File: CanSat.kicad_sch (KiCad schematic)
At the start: 44 parts, among them IC1 W25Q128JVPIQ, J1 USB_C_Receptacle, J10 Conn_01x04_Pin, J2 Conn_Coaxial, J3 Conn_01x06_Socket, J4 Conn_01x02_Pin, J5 Screw_Terminal_01x02, J6 Conn_01x06_Pin, J7 Conn_01x03_Pin, J8 Conn_01x02_Pin, J9 Conn_01x02_Pin, SW1 SW_Push, SW2 SW_Push, U1 MPU-6050, U3 Waveshare23721, U4 RFM98W-433S2, U8 BMP280, U9 APS6404L-3SQR-ZR

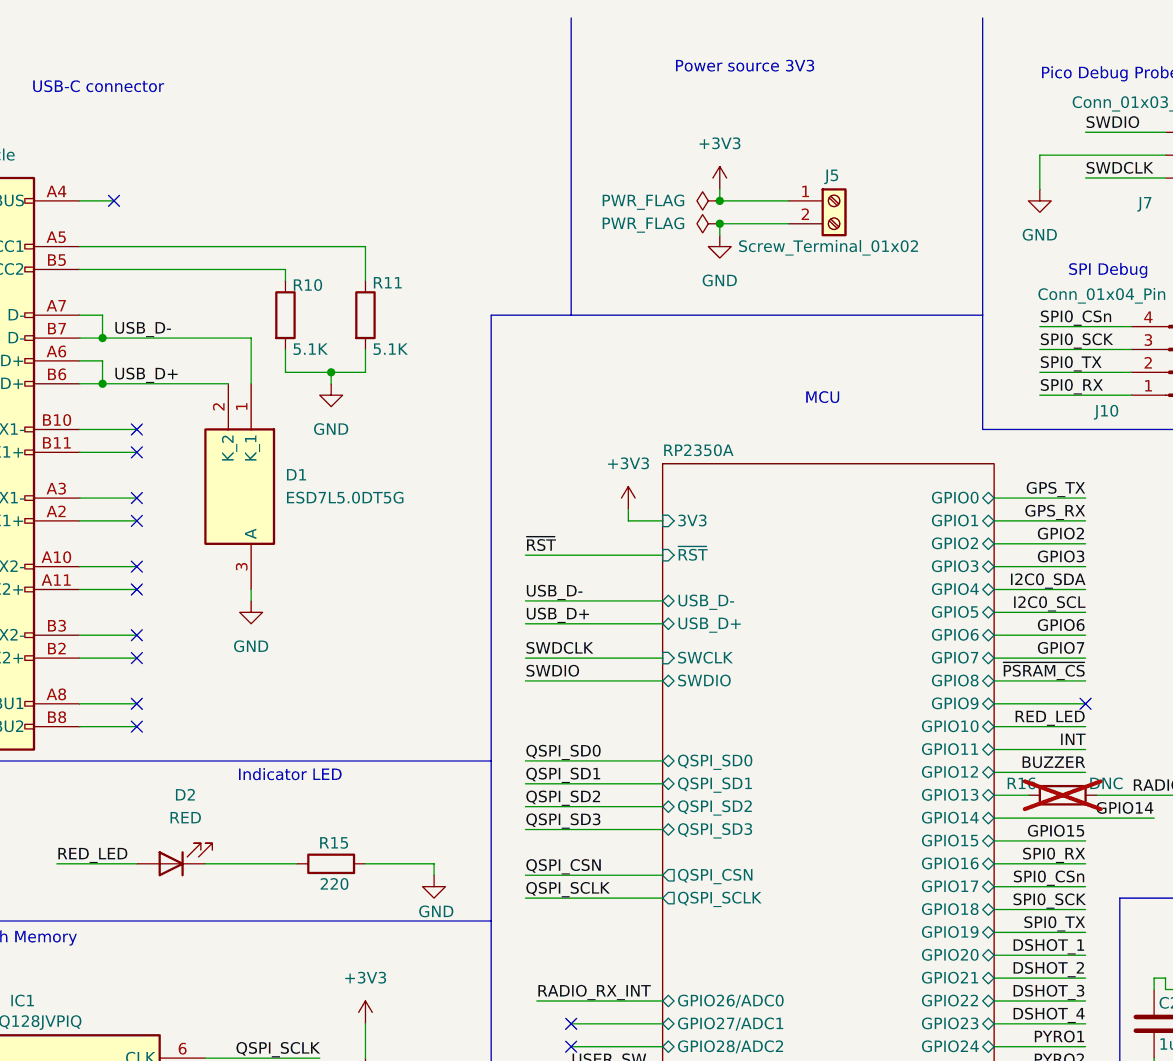
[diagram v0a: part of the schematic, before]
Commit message: Changed LoRa footprint + signed the PCB + added a on/off button
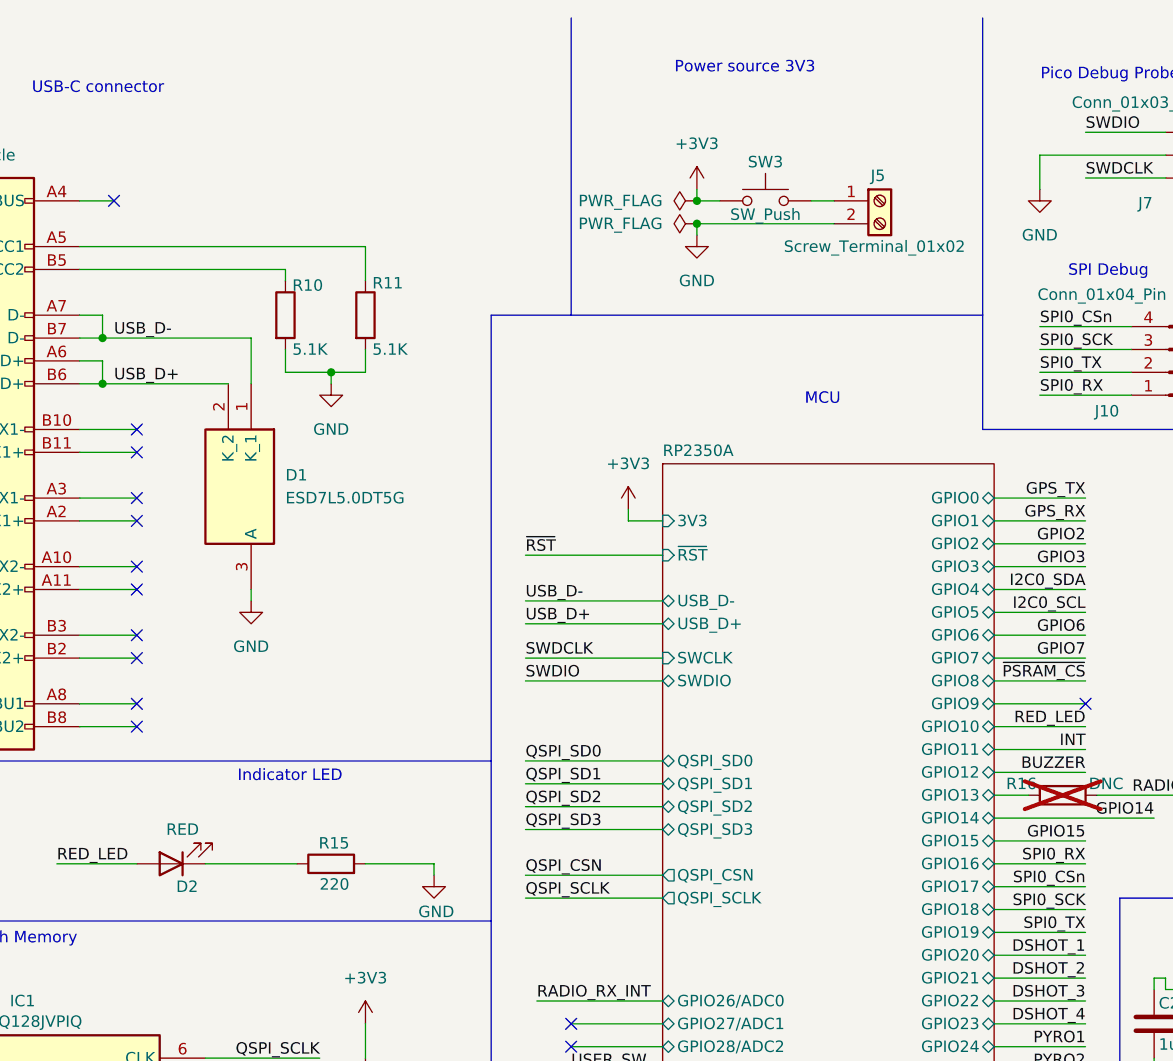
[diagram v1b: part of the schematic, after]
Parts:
- added SW3: SW_Push, Button_Switch_SMD:SW_Push_1P1T_NO_Vertical_Wuerth_434133025816, symbol Switch:SW_Push
- U4: footprint RF_Module:HOPERF_RFM9XW_THT -> RF_Module:HOPERF_RFM9XW_SMD
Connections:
- net +3V3: now also SW3.1; no longer J5.1 (Pin_1)
- new net: J5.1 (Pin_1), SW3.2
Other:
- moved on the sheet: J5
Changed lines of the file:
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@@
 	(title_block
 		(title "Main Board")
-		(date "2026-01-26")
-		(rev "v2.0.0")
+		(date "2026-03-07")
+		(rev "v2.1.0")
 		(company "Team ApolLO")
 		(comment 1 "Author: Wiktor Kociuba")
@@
 	)
 	(junction
-		(at 123.19 35.56)
+		(at 120.65 35.56)
 		(diameter 0)
 		(color 0 0 0 0)
@@
 	)
 	(junction
-		(at 123.19 33.02)
-		(diameter 0)
-		(color 0 0 0 0)
-	)
-	(junction
 		(at 179.07 120.65)
 		(diameter 0)
@@
 	)
 	(junction
+		(at 120.65 33.02)
+		(diameter 0)
+		(color 0 0 0 0)
+	)
+	(junction
 		(at 233.68 120.65)
 		(diameter 0)
@@
 	(wire
 		(pts
-			(xy 123.19 31.75) (xy 123.19 33.02)
+			(xy 120.65 31.75) (xy 120.65 33.02)
 		)
 		(stroke
@@
 	(wire
 		(pts
-			(xy 123.19 35.56) (xy 123.19 36.83)
+			(xy 120.65 35.56) (xy 120.65 36.83)
 		)
 		(stroke
@@
 	(wire
 		(pts
+			(xy 133.35 33.02) (xy 135.89 33.02)
+		)
+		(stroke
+			(width 0)
+			(type default)
+		)
+	)
+	(wire
+		(pts
 			(xy 247.65 158.75) (xy 245.11 158.75)
 		)
@@
 	(wire
 		(pts
-			(xy 123.19 33.02) (xy 130.81 33.02)
-		)
-		(stroke
-			(width 0)
-			(type default)
-		)
-	)
-	(wire
-		(pts
 			(xy 185.42 30.48) (xy 193.04 30.48)
 		)
@@
 	(wire
 		(pts
+			(xy 120.65 33.02) (xy 123.19 33.02)
+		)
+		(stroke
+			(width 0)
+			(type default)
+		)
+	)
+	(wire
+		(pts
 			(xy 213.36 86.36) (xy 213.36 93.98)
 		)
@@
 	(wire
 		(pts
-			(xy 123.19 35.56) (xy 130.81 35.56)
+			(xy 120.65 35.56) (xy 135.89 35.56)
 		)
 		(stroke
@@
 	(symbol
 		(lib_id "power:GND")
-		(at 123.19 36.83 0)
+		(at 120.65 36.83 0)
 		(unit 1)
 		(exclude_from_sim no)
@@
 		(fields_autoplaced yes)
 		(property "Reference" "#PWR07"
-			(at 123.19 43.18 0)
+			(at 120.65 43.18 0)
 			(effects
 				(font
@@
 		)
 		(property "Value" "GND"
-			(at 123.19 41.91 0)
+			(at 120.65 41.91 0)
 			(effects
 				(font
@@
 		)
 		(property "Footprint" ""
-			(at 123.19 36.83 0)
+			(at 120.65 36.83 0)
 			(effects
 				(font
@@
 		)
 		(property "Datasheet" ""
-			(at 123.19 36.83 0)
+			(at 120.65 36.83 0)
 			(effects
 				(font
@@
 		)
 		(property "Description" "Power symbol creates a global label with name \"GND\" , ground"
-			(at 123.19 36.83 0)
+			(at 120.65 36.83 0)
 			(effects
 				(font
@@
 	(symbol
 		(lib_id "Connector:Screw_Terminal_01x02")
-		(at 135.89 33.02 0)
+		(at 140.97 33.02 0)
 		(unit 1)
 		(exclude_from_sim no)
@@
 		(dnp no)
 		(property "Reference" "J5"
-			(at 134.874 30.226 0)
+			(at 139.954 30.226 0)
 			(effects
 				(font
@@
 		)
 		(property "Value" "Screw_Terminal_01x02"
-			(at 125.222 38.1 0)
+			(at 130.302 38.1 0)
 			(effects
 				(font
@@
 		)
 		(property "Footprint" "TerminalBlock:TerminalBlock_bornier-2_P5.08mm"
-			(at 135.89 33.02 0)
+			(at 140.97 33.02 0)
 			(effects
 				(font
@@
 		)
 		(property "Datasheet" "~"
-			(at 135.89 33.02 0)
+			(at 140.97 33.02 0)
 			(effects
 				(font
@@
 		)
 		(property "Description" "Generic screw terminal, single row, 01x02, script generated (kicad-library-utils/schlib/autogen/connector/)"
-			(at 135.89 33.02 0)
+			(at 140.97 33.02 0)
 			(effects
 				(font
@@
 		(on_board yes)
 		(dnp no)
-		(fields_autoplaced yes)
 		(property "Reference" "D2"
-			(at 63.8175 99.06 0)
+			(at 64.008 109.22 0)
 			(effects
 				(font
@@
 		)
 		(property "Value" "RED"
-			(at 63.8175 101.6 0)
+			(at 63.5 102.87 0)
 			(effects
 				(font
@@
 			)
 		)
-		(property "Footprint" "RF_Module:HOPERF_RFM9XW_THT"
+		(property "Footprint" "RF_Module:HOPERF_RFM9XW_SMD"
 			(at 161.29 100.33 0)
 			(effects
@@
 	(symbol
 		(lib_id "power:PWR_FLAG")
-		(at 123.19 35.56 90)
+		(at 120.65 35.56 90)
 		(unit 1)
 		(exclude_from_sim no)
@@
 		(fields_autoplaced yes)
 		(property "Reference" "#FLG02"
-			(at 121.285 35.56 0)
+			(at 118.745 35.56 0)
 			(effects
 				(font
@@
 		)
 		(property "Value" "PWR_FLAG"
-			(at 119.38 35.5599 90)
+			(at 116.84 35.5599 90)
 			(effects
 				(font
@@
 		)
 		(property "Footprint" ""
-			(at 123.19 35.56 0)
+			(at 120.65 35.56 0)
 			(effects
 				(font
@@
 		)
 		(property "Datasheet" "~"
-			(at 123.19 35.56 0)
+			(at 120.65 35.56 0)
 			(effects
 				(font
@@
 		)
 		(property "Description" "Special symbol for telling ERC where power comes from"
-			(at 123.19 35.56 0)
+			(at 120.65 35.56 0)
 			(effects
 				(font
@@
 	)
 	(symbol
+		(lib_id "Switch:SW_Push")
+		(at 128.27 33.02 0)
+		(unit 1)
+		(exclude_from_sim no)
+		(in_bom yes)
+		(on_board yes)
+		(dnp no)
+		(property "Reference" "SW3"
+			(at 128.27 28.702 0)
+			(effects
+				(font
+					(size 1.27 1.27)
+				)
+			)
+		)
+		(property "Value" "SW_Push"
+			(at 128.27 34.544 0)
+			(effects
+				(font
+					(size 1.27 1.27)
+				)
+			)
+		)
+		(property "Footprint" "Button_Switch_SMD:SW_Push_1P1T_NO_Vertical_Wuerth_434133025816"
+			(at 128.27 27.94 0)
+			(effects
+				(font
+					(size 1.27 1.27)
+				)
+				(hide yes)
+			)
+		)
+		(property "Datasheet" "~"
+			(at 128.27 27.94 0)
+			(effects
+				(font
+					(size 1.27 1.27)
+				)
+				(hide yes)
+			)
+		)
+		(property "Description" "Push button switch, generic, two pins"
+			(at 128.27 33.02 0)
+			(effects
+				(font
+					(size 1.27 1.27)
+				)
+				(hide yes)
+			)
+		)
+		(pin "2"
+		)
+		(pin "1"
+		)
+		(instances
+			(project ""
+				(path "/c5feb985-eaed-4048-a722-7becddf33f05"
+					(reference "SW3")
+					(unit 1)
+				)
+			)
+		)
+	)
+	(symbol
 		(lib_id "power:+3V3")
 		(at 113.03 67.31 0)
@@
 	(symbol
 		(lib_id "power:+3V3")
-		(at 123.19 31.75 0)
+		(at 120.65 31.75 0)
 		(unit 1)
 		(exclude_from_sim no)
@@
 		(fields_autoplaced yes)
 		(property "Reference" "#PWR08"
-			(at 123.19 35.56 0)
+			(at 120.65 35.56 0)
 			(effects
 				(font
@@
 		)
 		(property "Value" "+3V3"
-			(at 123.19 26.67 0)
+			(at 120.65 26.67 0)
 			(effects
 				(font
@@
 		)
 		(property "Footprint" ""
-			(at 123.19 31.75 0)
+			(at 120.65 31.75 0)
 			(effects
 				(font
@@
 		)
 		(property "Datasheet" ""
-			(at 123.19 31.75 0)
+			(at 120.65 31.75 0)
 			(effects
 				(font
@@
 		)
 		(property "Description" "Power symbol creates a global label with name \"+3V3\""
-			(at 123.19 31.75 0)
+			(at 120.65 31.75 0)
 			(effects
 				(font
@@
 	(symbol
 		(lib_id "power:PWR_FLAG")
-		(at 123.19 33.02 90)
+		(at 120.65 33.02 90)
 		(unit 1)
 		(exclude_from_sim no)
@@
 		(fields_autoplaced yes)
 		(property "Reference" "#FLG01"
-			(at 121.285 33.02 0)
+			(at 118.745 33.02 0)
 			(effects
 				(font
@@
 		)
 		(property "Value" "PWR_FLAG"
-			(at 119.38 33.0199 90)
+			(at 116.84 33.0199 90)
 			(effects
 				(font
@@
 		)
 		(property "Footprint" ""
-			(at 123.19 33.02 0)
+			(at 120.65 33.02 0)
 			(effects
 				(font
@@
 		)
 		(property "Datasheet" "~"
-			(at 123.19 33.02 0)
+			(at 120.65 33.02 0)
 			(effects
 				(font
@@
 		)
 		(property "Description" "Special symbol for telling ERC where power comes from"
-			(at 123.19 33.02 0)
+			(at 120.65 33.02 0)
 			(effects
 				(font

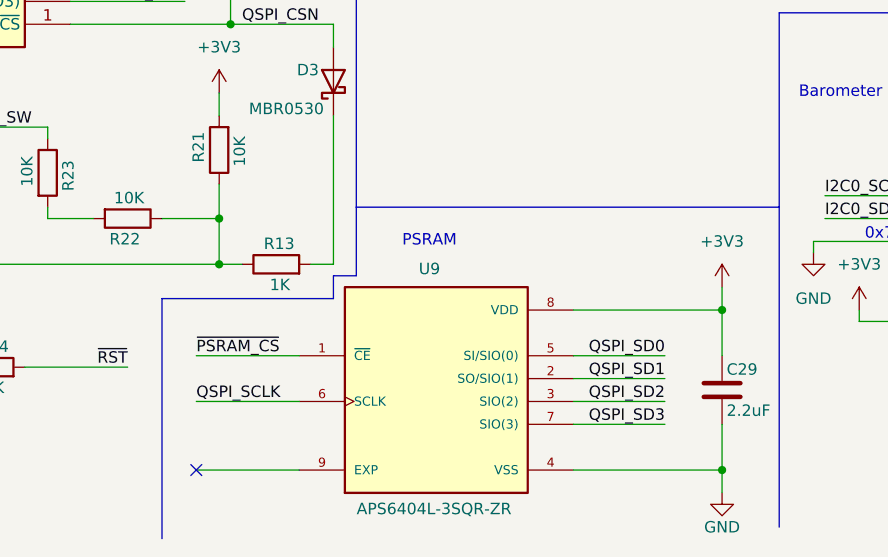
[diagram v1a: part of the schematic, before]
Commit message: Fixed design flaw with with components that MCU depends on
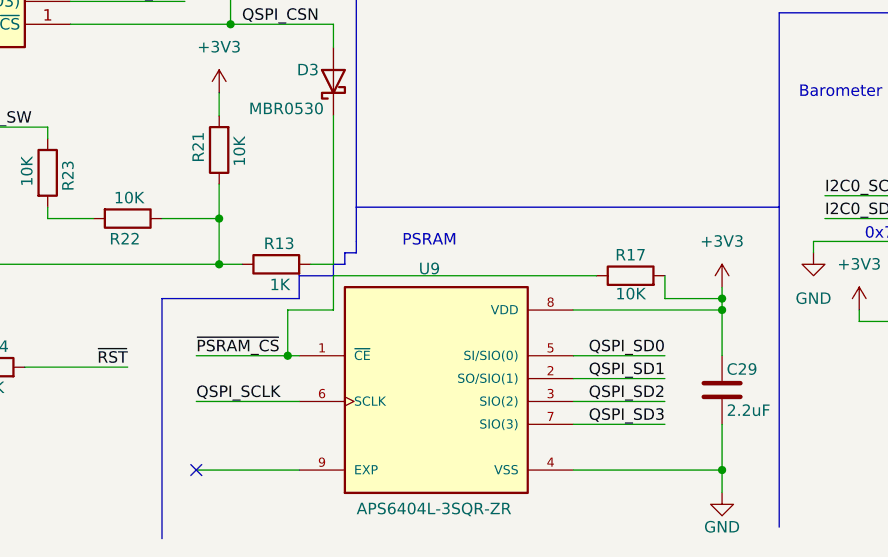
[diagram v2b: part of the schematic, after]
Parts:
- added R17: 10K, Resistor_SMD:R_0402_1005Metric, symbol Device:R
- BZ1: footprint Buzzer_Beeper:MagneticBuzzer_Kingstate_KCG0601 -> buzzer:CMT-4023S
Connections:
- net +3V3: now also R17.2
- net ~{PSRAM_CS}: now also R17.1
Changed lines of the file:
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@@
 	(title_block
 		(title "Main Board")
-		(date "2026-03-07")
-		(rev "v2.1.0")
+		(date "2026-03-11")
+		(rev "v2.1.1")
 		(company "Team ApolLO")
 		(comment 1 "Author: Wiktor Kociuba")
@@
 	)
 	(junction
+		(at 138.43 171.45)
+		(diameter 0)
+		(color 0 0 0 0)
+	)
+	(junction
 		(at 245.11 158.75)
 		(diameter 0)
@@
 	)
 	(junction
+		(at 90.17 177.8)
+		(diameter 0)
+		(color 0 0 0 0)
+	)
+	(junction
 		(at 82.55 167.64)
 		(diameter 0)
@@
 	(wire
 		(pts
+			(xy 132.08 168.91) (xy 132.08 171.45)
+		)
+		(stroke
+			(width 0)
+			(type default)
+		)
+	)
+	(wire
+		(pts
 			(xy 185.42 81.28) (xy 194.31 81.28)
 		)
@@
 	(wire
 		(pts
+			(xy 90.17 172.72) (xy 95.25 172.72)
+		)
+		(stroke
+			(width 0)
+			(type default)
+		)
+	)
+	(wire
+		(pts
 			(xy 66.04 138.43) (xy 78.74 138.43)
 		)
@@
 	(wire
 		(pts
+			(xy 95.25 168.91) (xy 124.46 168.91)
+		)
+		(stroke
+			(width 0)
+			(type default)
+		)
+	)
+	(wire
+		(pts
 			(xy 245.11 158.75) (xy 245.11 160.02)
 		)
@@
 	(polyline
 		(pts
-			(xy 76.2 171.45) (xy 95.25 171.45)
+			(xy 76.2 171.45) (xy 91.44 171.45)
 		)
 		(stroke
@@
 	(polyline
 		(pts
-			(xy 97.79 168.91) (xy 97.79 161.29)
+			(xy 97.79 165.1) (xy 97.79 161.29)
+		)
+		(stroke
+			(width 0)
+			(type default)
+		)
+	)
+	(polyline
+		(pts
+			(xy 96.52 166.37) (xy 97.79 166.37)
 		)
 		(stroke
@@
 	(polyline
 		(pts
-			(xy 95.25 171.45) (xy 95.25 168.91)
+			(xy 91.44 171.45) (xy 91.44 168.91)
 		)
 		(stroke
@@
 	(wire
 		(pts
+			(xy 138.43 171.45) (xy 138.43 172.72)
+		)
+		(stroke
+			(width 0)
+			(type default)
+		)
+	)
+	(wire
+		(pts
 			(xy 36.83 167.64) (xy 36.83 179.07)
 		)
@@
 	(wire
 		(pts
+			(xy 90.17 177.8) (xy 90.17 172.72)
+		)
+		(stroke
+			(width 0)
+			(type default)
+		)
+	)
+	(wire
+		(pts
 			(xy 170.18 175.26) (xy 170.18 176.53)
 		)
@@
 	(wire
 		(pts
-			(xy 80.01 177.8) (xy 91.44 177.8)
+			(xy 80.01 177.8) (xy 90.17 177.8)
 		)
 		(stroke
@@
 	(wire
 		(pts
+			(xy 95.25 172.72) (xy 95.25 168.91)
+		)
+		(stroke
+			(width 0)
+			(type default)
+		)
+	)
+	(wire
+		(pts
 			(xy 153.67 71.12) (xy 163.83 71.12)
 		)
@@
 		)
 	)
+	(polyline
+		(pts
+			(xy 95.25 168.91) (xy 95.25 167.64)
+		)
+		(stroke
+			(width 0)
+			(type default)
+		)
+	)
 	(wire
 		(pts
@@
 	(wire
 		(pts
+			(xy 90.17 177.8) (xy 91.44 177.8)
+		)
+		(stroke
+			(width 0)
+			(type default)
+		)
+	)
+	(wire
+		(pts
 			(xy 200.66 152.4) (xy 208.28 152.4)
 		)
@@
 	(wire
 		(pts
+			(xy 132.08 171.45) (xy 138.43 171.45)
+		)
+		(stroke
+			(width 0)
+			(type default)
+		)
+	)
+	(wire
+		(pts
 			(xy 24.13 138.43) (xy 22.86 138.43)
 		)
@@
 		)
 	)
-	(polyline
+	(wire
 		(pts
-			(xy 95.25 168.91) (xy 97.79 168.91)
+			(xy 185.42 27.94) (xy 193.04 27.94)
 		)
 		(stroke
@@
 		)
 	)
-	(wire
+	(polyline
 		(pts
-			(xy 185.42 27.94) (xy 193.04 27.94)
+			(xy 96.52 167.64) (xy 96.52 166.37)
 		)
 		(stroke
@@
 		)
 	)
+	(polyline
+		(pts
+			(xy 91.44 168.91) (xy 95.25 168.91)
+		)
+		(stroke
+			(width 0)
+			(type default)
+		)
+	)
 	(wire
 		(pts
@@
 		)
 	)
+	(polyline
+		(pts
+			(xy 95.25 167.64) (xy 96.52 167.64)
+		)
+		(stroke
+			(width 0)
+			(type default)
+		)
+	)
 	(wire
 		(pts
@@
 		)
 	)
+	(polyline
+		(pts
+			(xy 97.79 166.37) (xy 97.79 165.1)
+		)
+		(stroke
+			(width 0)
+			(type default)
+		)
+	)
 	(wire
 		(pts
@@
 	(wire
 		(pts
-			(xy 138.43 170.18) (xy 138.43 172.72)
+			(xy 138.43 170.18) (xy 138.43 171.45)
 		)
 		(stroke
@@
 			)
 		)
-		(property "Footprint" "Buzzer_Beeper:MagneticBuzzer_Kingstate_KCG0601"
+		(property "Footprint" "buzzer:CMT-4023S"
 			(at 266.065 25.4 90)
 			(effects
@@
 					(unit 1)
 				)
+			)
+		)
+	)
+	(symbol
+		(lib_id "Device:R")
+		(at 128.27 168.91 90)
+		(unit 1)
+		(exclude_from_sim no)
+		(in_bom yes)
+		(on_board yes)
+		(dnp no)
+		(property "Reference" "R17"
+			(at 128.27 166.624 90)
+			(effects
+				(font
+					(size 1.27 1.27)
+				)
+			)
+		)
+		(property "Value" "10K"
+			(at 128.27 170.942 90)
+			(effects
+				(font
+					(size 1.27 1.27)
+				)
+			)
+		)
+		(property "Footprint" "Resistor_SMD:R_0402_1005Metric"
+			(at 128.27 170.688 90)
+			(effects
+				(font
+					(size 1.27 1.27)
+				)
+				(hide yes)
+			)
+		)
+		(property "Datasheet" "~"
+			(at 128.27 168.91 0)
+			(effects
+				(font
+					(size 1.27 1.27)
+				)
+				(hide yes)
+			)
+		)
+		(property "Description" "Resistor"
+			(at 128.27 168.91 0)
+			(effects
+				(font
+					(size 1.27 1.27)
+				)
+				(hide yes)
+			)
+		)
+		(pin "1"
+		)
+		(pin "2"
+		)
+		(instances
+			(project ""
+				(path "/c5feb985-eaed-4048-a722-7becddf33f05"
+					(reference "R17")
+					(unit 1)
+				)
